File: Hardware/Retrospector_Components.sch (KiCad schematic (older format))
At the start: 148 parts, among them J1 Conn_01x08_Male, J2 Conn_01x08_Male, J3 Conn_01x08_Male, J4 Conn_01x08_Male, J5 SWD_Header, J6 USB_B_Micro, J7 Eurorack_10_pin_power, J8 I2C_TestPoint, U1 MCP6004, U10 LD1117-3.3-4Tab, U2 TL074, U3 MCP6004, U4 IS42S16800F-7TLI, U5 STM32H743ZITx, U6 TL072, U7 AS3364, U8 PCM5100APW, U9 LM2675M-5, Y1 8MHz 20pF

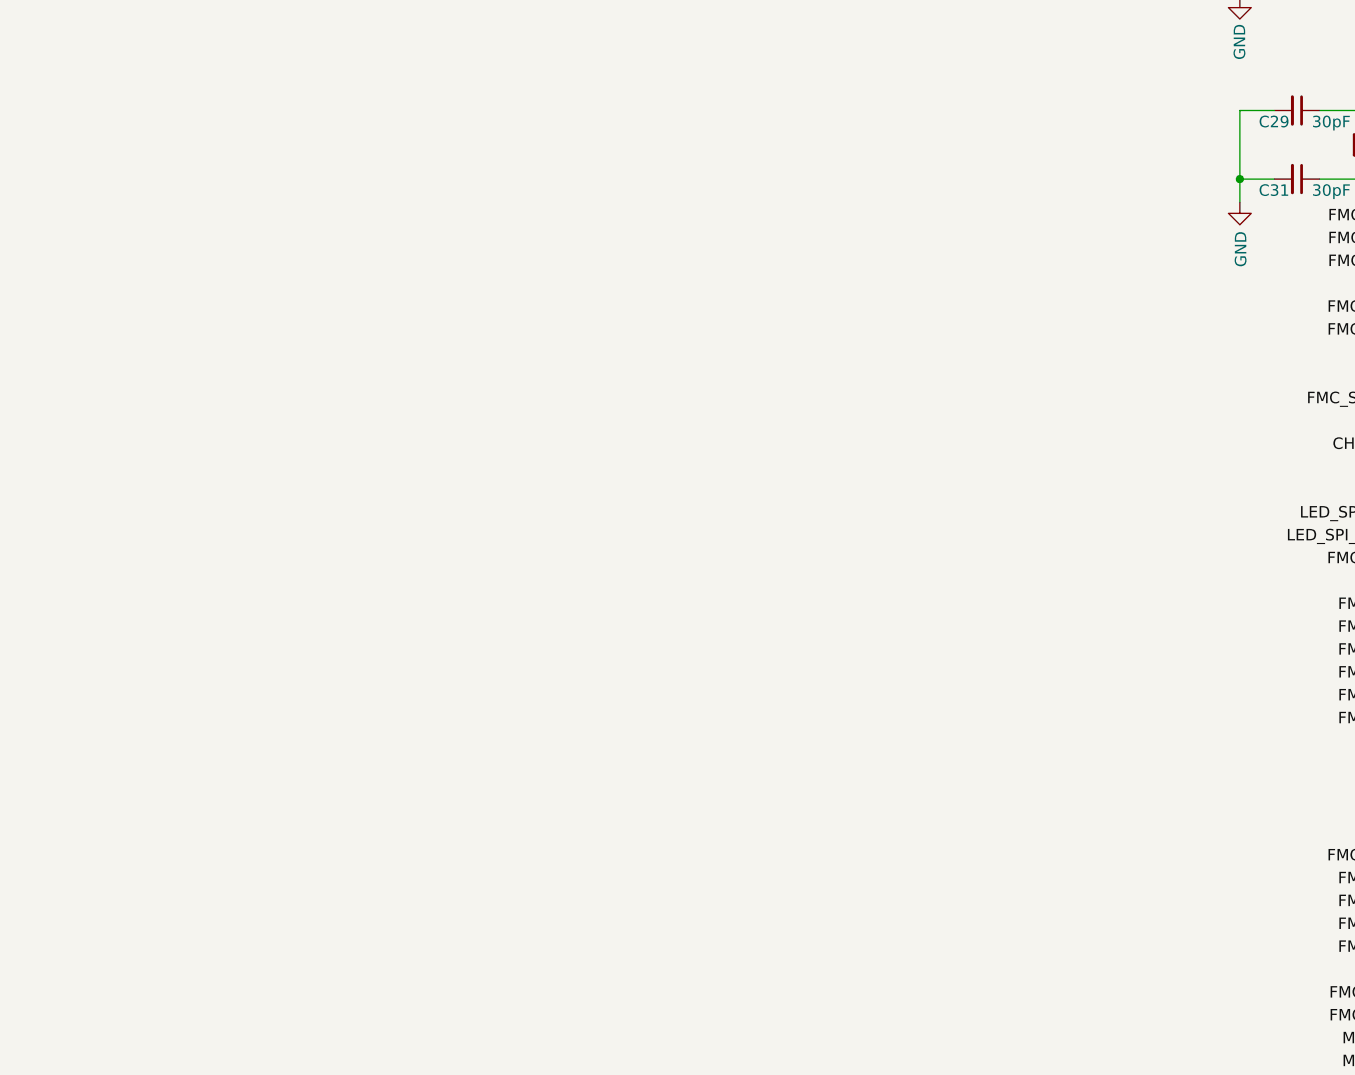
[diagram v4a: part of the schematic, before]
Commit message: Debugging ADC issues
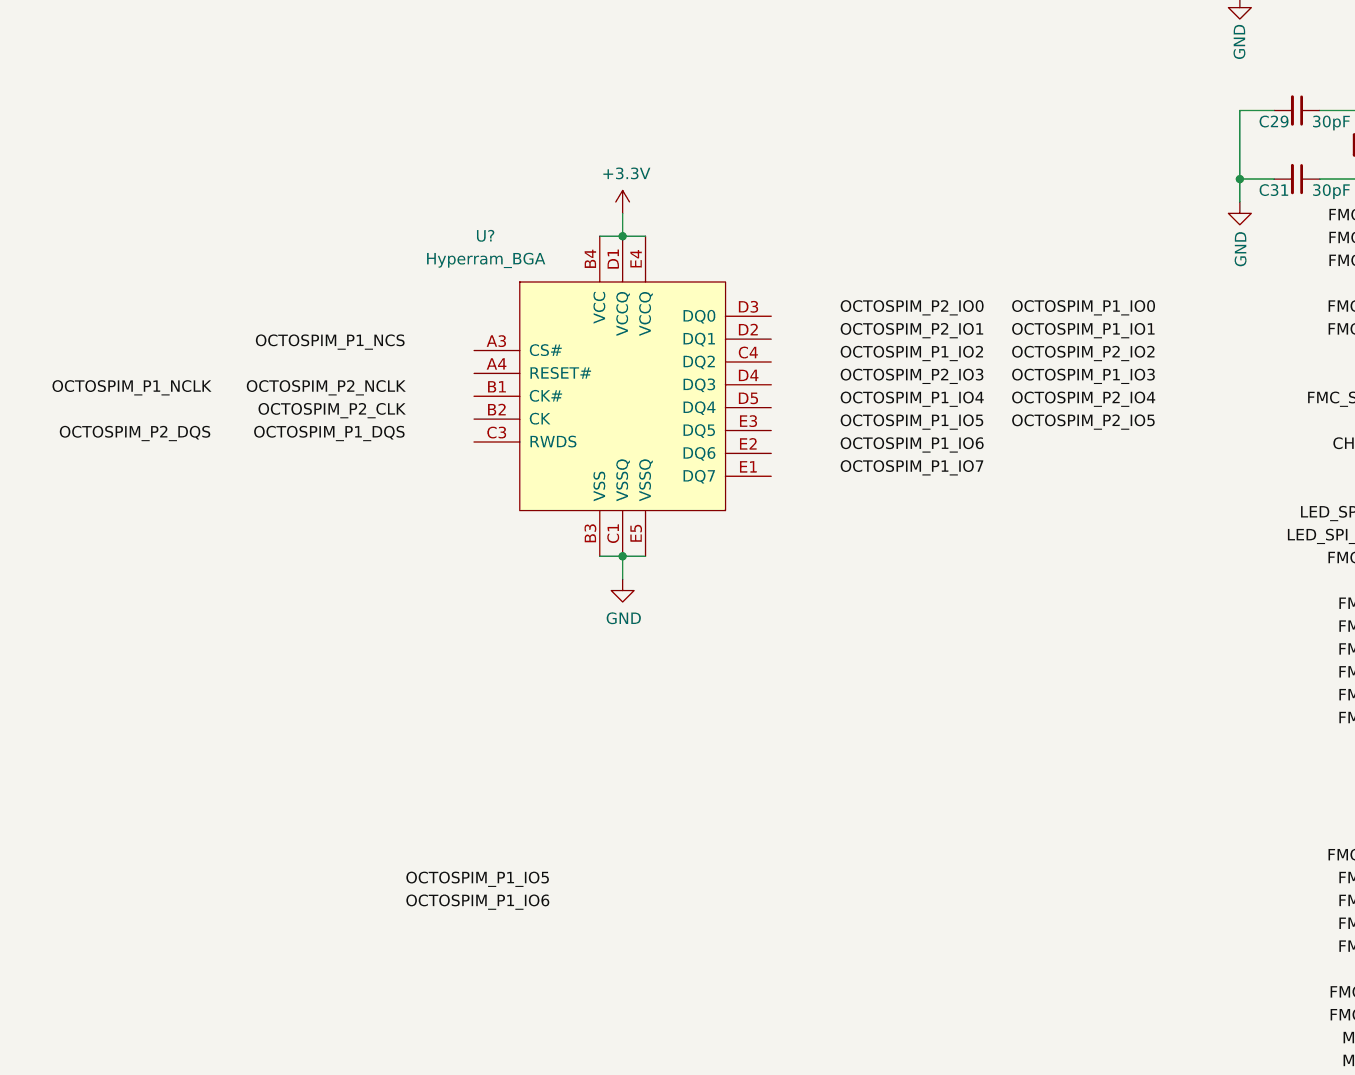
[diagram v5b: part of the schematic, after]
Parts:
- added U?: Hyperram_BGA, symbol Hyperram:Hyperram_BGA
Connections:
- net +3V3: now also U?.B4 (VCC), U?.D1 (VCCQ), U?.E4 (VCCQ)
- net GND: now also U?.B3 (VSS), U?.C1 (VSSQ), U?.E5 (VSSQ)
- new net: U?.A2 (RFU), U?.A5 (RFU), U?.B5 (RFU), U?.C2 (RFU), U?.C5 (RFU)
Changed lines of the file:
@@
 Wire Wire Line
 	1750 3850 1600 3850
+$Comp
+L Hyperram:Hyperram_BGA U?
+U 1 1 6081A4E3
+P -1800 3950
+F 0 "U?" H -2400 4200 50  0000 C CNN
+F 1 "Hyperram_BGA" H -2400 4100 50  0000 C CNN
+F 2 "" H -1950 4150 50  0001 C CNN
+F 3 "" H -1950 4150 50  0001 C CNN
+	1    -1800 3950
+	1    0    0    -1
+$EndComp
+$Comp
+L power:+3.3V #PWR?
+U 1 1 6081CB90
+P -1800 3600
+F 0 "#PWR?" H -1800 3450 50  0001 C CNN
+F 1 "+3.3V" H -1785 3773 50  0000 C CNN
+F 2 "" H -1800 3600 50  0001 C CNN
+F 3 "" H -1800 3600 50  0001 C CNN
+	1    -1800 3600
+	1    0    0    -1
+$EndComp
+Wire Wire Line
+	-1900 3700 -1800 3700
+Connection ~ -1800 3700
+Wire Wire Line
+	-1800 3700 -1700 3700
+Wire Wire Line
+	-1800 3700 -1800 3600
+$Comp
+L power:GND #PWR?
+U 1 1 6099F694
+P -1800 5200
+F 0 "#PWR?" H -1800 4950 50  0001 C CNN
+F 1 "GND" H -1795 5027 50  0000 C CNN
+F 2 "" H -1800 5200 50  0001 C CNN
+F 3 "" H -1800 5200 50  0001 C CNN
+	1    -1800 5200
+	1    0    0    -1
+$EndComp
+Wire Wire Line
+	-1900 5100 -1800 5100
+Connection ~ -1800 5100
+Wire Wire Line
+	-1800 5100 -1700 5100
+Wire Wire Line
+	-1800 5100 -1800 5200
+Text Label -850 4250 0    50   ~ 0
+OCTOSPIM_P1_IO2
+Text Label -850 4050 0    50   ~ 0
+OCTOSPIM_P2_IO0
+Text Label -850 4150 0    50   ~ 0
+OCTOSPIM_P2_IO1
+Text Label -100 4250 0    50   ~ 0
+OCTOSPIM_P2_IO2
+Text Label -850 4350 0    50   ~ 0
+OCTOSPIM_P2_IO3
+Text Label -2750 4500 2    50   ~ 0
+OCTOSPIM_P2_CLK
+Text Label -2750 4400 2    50   ~ 0
+OCTOSPIM_P2_NCLK
+Text Label -100 4350 0    50   ~ 0
+OCTOSPIM_P1_IO3
+Text Label -100 4050 0    50   ~ 0
+OCTOSPIM_P1_IO0
+Text Label -100 4150 0    50   ~ 0
+OCTOSPIM_P1_IO1
+Text Label -850 4450 0    50   ~ 0
+OCTOSPIM_P1_IO4
+Text Label -2750 6550 0    50   ~ 0
+OCTOSPIM_P1_IO5
+Text Label -2750 6650 0    50   ~ 0
+OCTOSPIM_P1_IO6
+Text Label -2750 4600 2    50   ~ 0
+OCTOSPIM_P1_DQS
+Text Label -3600 4400 2    50   ~ 0
+OCTOSPIM_P1_NCLK
+Text Label -3600 4600 2    50   ~ 0
+OCTOSPIM_P2_DQS
+Text Label -100 4450 0    50   ~ 0
+OCTOSPIM_P2_IO4
+Text Label -100 4550 0    50   ~ 0
+OCTOSPIM_P2_IO5
+Text Label -850 4550 0    50   ~ 0
+OCTOSPIM_P1_IO5
+Text Label -850 4650 0    50   ~ 0
+OCTOSPIM_P1_IO6
+Text Label -850 4750 0    50   ~ 0
+OCTOSPIM_P1_IO7
+Text Label -2750 4200 2    50   ~ 0
+OCTOSPIM_P1_NCS
 $EndSCHEMATC

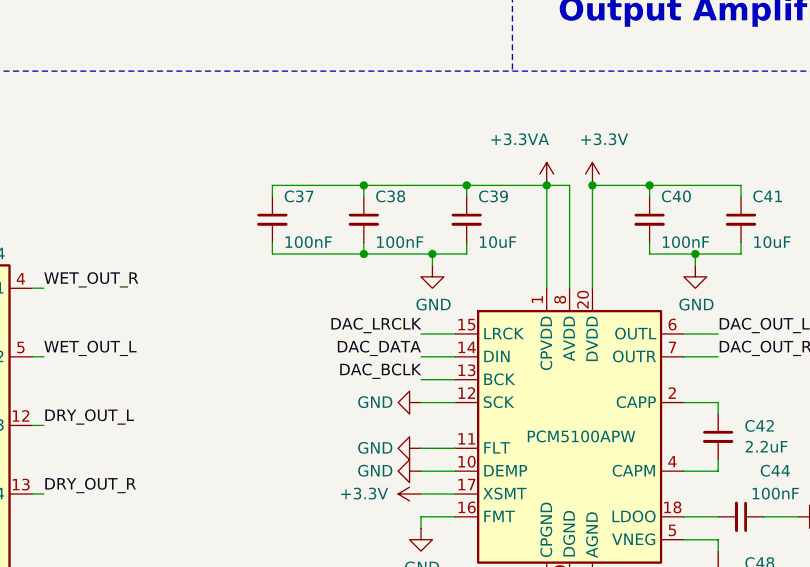
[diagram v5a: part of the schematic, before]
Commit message: Various tests for ADC accuracy
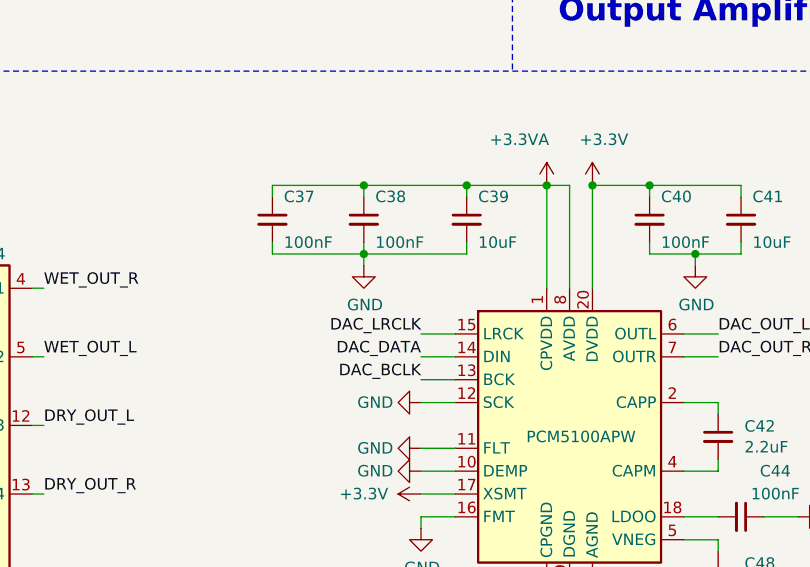
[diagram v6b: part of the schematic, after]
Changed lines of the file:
@@
 Wire Wire Line
 	13150 8600 13150 8550
-Wire Wire Line
-	13150 8850 13450 8850
 Connection ~ 13150 8850
 Wire Wire Line
@@
 L power:GND #PWR044
 U 1 1 5ED6422C
-P 13450 8900
-F 0 "#PWR044" H 13450 8650 50  0001 C CNN
-F 1 "GND" H 13455 8727 50  0000 C CNN
-F 2 "" H 13450 8900 50  0001 C CNN
-F 3 "" H 13450 8900 50  0001 C CNN
-	1    13450 8900
+P 13150 8900
+F 0 "#PWR044" H 13150 8650 50  0001 C CNN
+F 1 "GND" H 13155 8727 50  0000 C CNN
+F 2 "" H 13150 8900 50  0001 C CNN
+F 3 "" H 13150 8900 50  0001 C CNN
+	1    13150 8900
 	1    0    0    -1
 $EndComp
@@
 	1    0    0    -1
 $EndComp
-Wire Wire Line
-	13450 8900 13450 8850
-Connection ~ 13450 8850
-Wire Wire Line
-	13450 8850 13600 8850
 Wire Wire Line
 	13950 8550 13950 9000
@@
 Text Label -2750 4200 2    50   ~ 0
 OCTOSPIM_P1_NCS
+Wire Wire Line
+	13150 8850 13600 8850
+Wire Wire Line
+	13150 8850 13150 8900
 $EndSCHEMATC

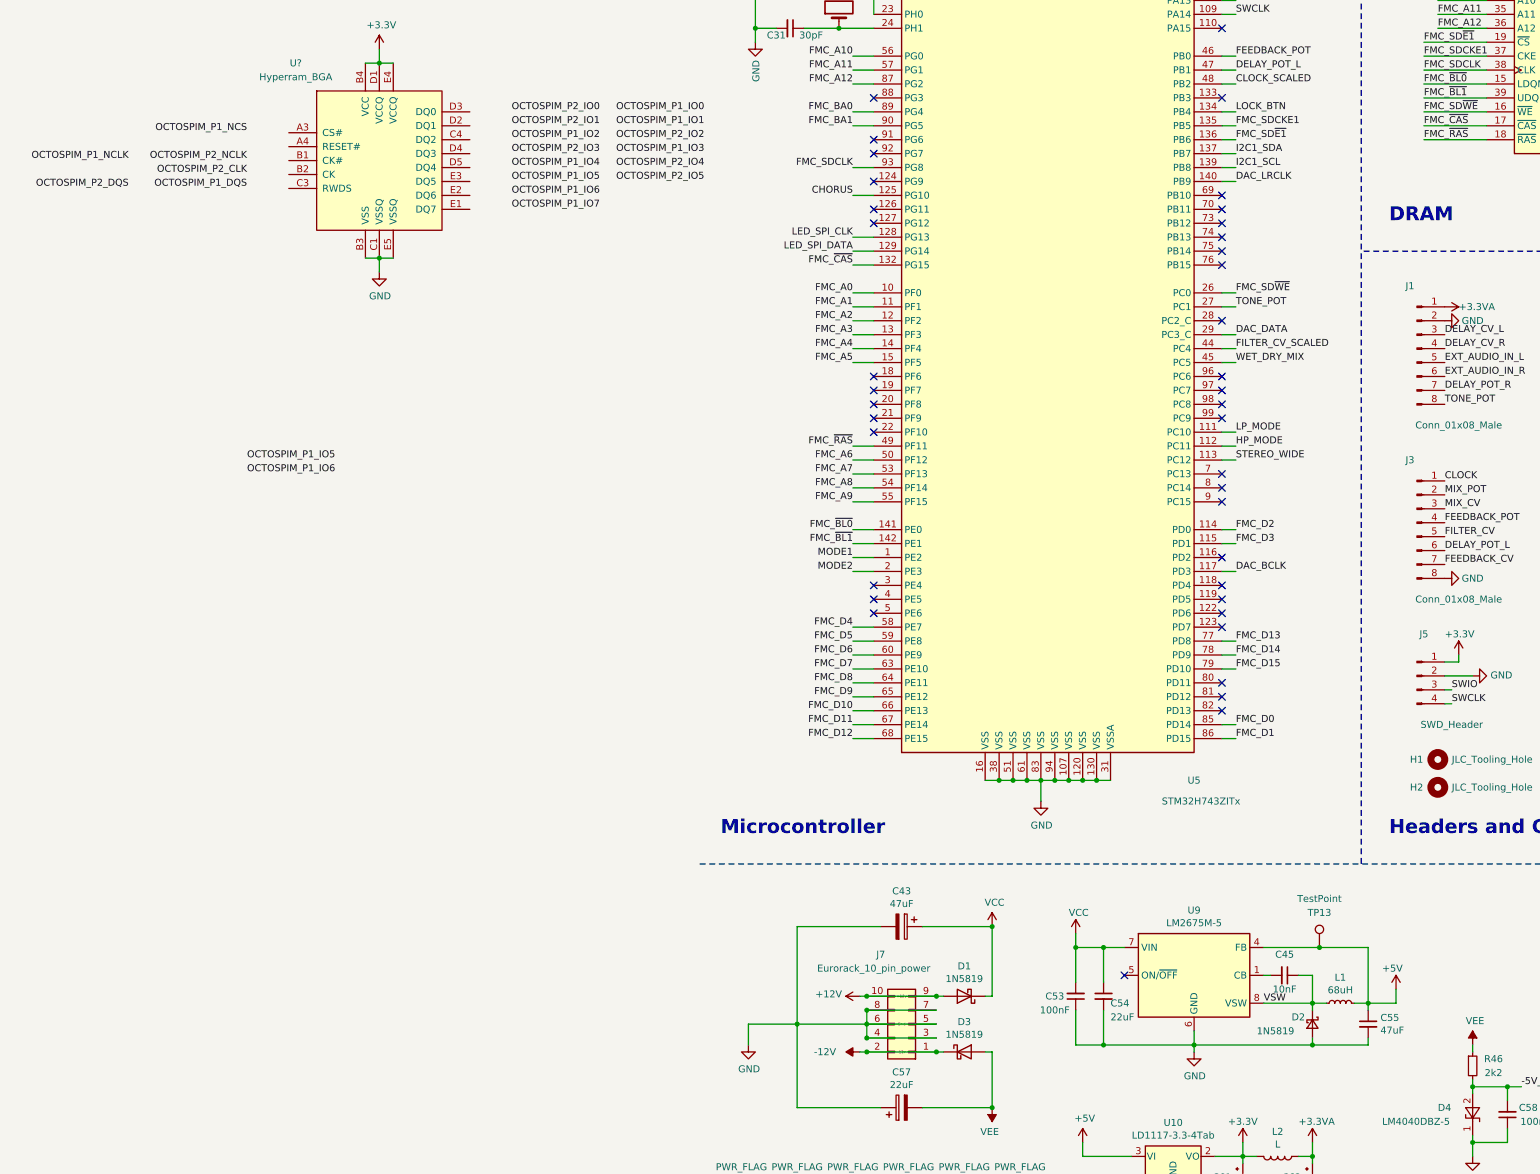
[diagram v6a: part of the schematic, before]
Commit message: Tweaks to LP filter settings; schematic
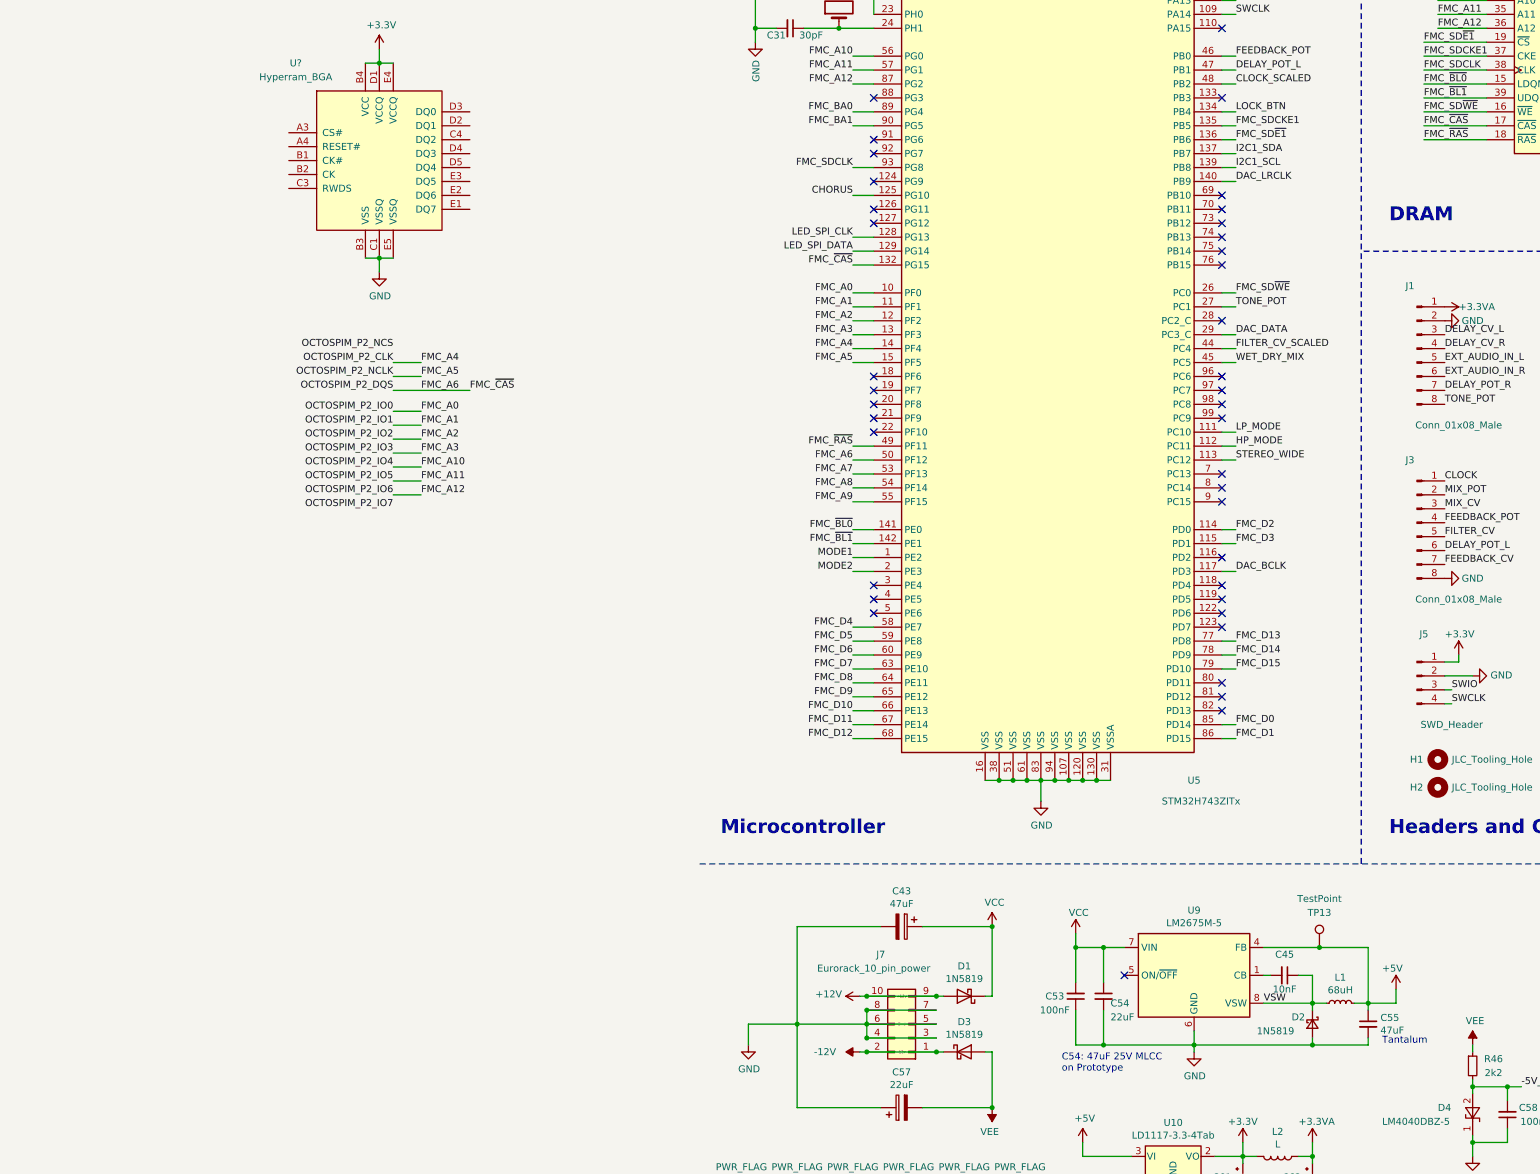
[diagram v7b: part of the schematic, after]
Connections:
- net FMC_~CAS is gone; now on net FMC_A6: U4.17 (~CAS), U5.132 (PG15)
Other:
- note added: "C54: 47uF 25V MLCC\non Prototype\n"
- note added: "Tantalum"
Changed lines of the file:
@@
 Wire Wire Line
 	-1800 5100 -1800 5200
-Text Label -850 4250 0    50   ~ 0
-OCTOSPIM_P1_IO2
-Text Label -850 4050 0    50   ~ 0
+Text Label -1700 6200 2    50   ~ 0
 OCTOSPIM_P2_IO0
-Text Label -850 4150 0    50   ~ 0
+Text Label -1700 6300 2    50   ~ 0
 OCTOSPIM_P2_IO1
-Text Label -100 4250 0    50   ~ 0
+Text Label -1700 6400 2    50   ~ 0
 OCTOSPIM_P2_IO2
-Text Label -850 4350 0    50   ~ 0
+Text Label -1700 6500 2    50   ~ 0
 OCTOSPIM_P2_IO3
-Text Label -2750 4500 2    50   ~ 0
+Text Label -1700 5850 2    50   ~ 0
 OCTOSPIM_P2_CLK
-Text Label -2750 4400 2    50   ~ 0
+Text Label -1700 5950 2    50   ~ 0
 OCTOSPIM_P2_NCLK
-Text Label -100 4350 0    50   ~ 0
-OCTOSPIM_P1_IO3
-Text Label -100 4050 0    50   ~ 0
-OCTOSPIM_P1_IO0
-Text Label -100 4150 0    50   ~ 0
-OCTOSPIM_P1_IO1
-Text Label -850 4450 0    50   ~ 0
-OCTOSPIM_P1_IO4
-Text Label -2750 6550 0    50   ~ 0
-OCTOSPIM_P1_IO5
-Text Label -2750 6650 0    50   ~ 0
-OCTOSPIM_P1_IO6
-Text Label -2750 4600 2    50   ~ 0
-OCTOSPIM_P1_DQS
-Text Label -3600 4400 2    50   ~ 0
-OCTOSPIM_P1_NCLK
-Text Label -3600 4600 2    50   ~ 0
+Text Label -1700 6050 2    50   ~ 0
 OCTOSPIM_P2_DQS
-Text Label -100 4450 0    50   ~ 0
+Text Label -1700 6600 2    50   ~ 0
 OCTOSPIM_P2_IO4
-Text Label -100 4550 0    50   ~ 0
+Text Label -1700 6700 2    50   ~ 0
 OCTOSPIM_P2_IO5
-Text Label -850 4550 0    50   ~ 0
-OCTOSPIM_P1_IO5
-Text Label -850 4650 0    50   ~ 0
-OCTOSPIM_P1_IO6
-Text Label -850 4750 0    50   ~ 0
-OCTOSPIM_P1_IO7
-Text Label -2750 4200 2    50   ~ 0
-OCTOSPIM_P1_NCS
 Wire Wire Line
 	13150 8850 13600 8850
 Wire Wire Line
 	13150 8850 13150 8900
+Text Notes 5400 10750 0    50   ~ 0
+Tantalum
+Text Notes 3100 10950 0    50   ~ 0
+C54: 47uF 25V MLCC\non Prototype\n
+Text Label -1700 6800 2    50   ~ 0
+OCTOSPIM_P2_IO6
+Text Label -1700 6900 2    50   ~ 0
+OCTOSPIM_P2_IO7
+Text Label -1700 5750 2    50   ~ 0
+OCTOSPIM_P2_NCS
+Text Label -1500 6200 0    50   ~ 0
+FMC_A0
+Text Label -1500 6300 0    50   ~ 0
+FMC_A1
+Text Label -1500 6400 0    50   ~ 0
+FMC_A2
+Text Label -1500 6500 0    50   ~ 0
+FMC_A3
+Text Label -1500 5850 0    50   ~ 0
+FMC_A4
+Text Label -1500 5950 0    50   ~ 0
+FMC_A5
+Text Label -1500 6050 0    50   ~ 0
+FMC_A6
+Text Label -1150 6050 0    50   ~ 0
+FMC_~CAS
+Text Label -1500 6600 0    50   ~ 0
+FMC_A10
+Text Label -1500 6700 0    50   ~ 0
+FMC_A11
+Text Label -1500 6800 0    50   ~ 0
+FMC_A12
+Wire Wire Line
+	-1700 5850 -1500 5850
+Wire Wire Line
+	-1700 5950 -1500 5950
+Wire Wire Line
+	-1700 6200 -1500 6200
+Wire Wire Line
+	-1700 6300 -1500 6300
+Wire Wire Line
+	-1700 6400 -1500 6400
+Wire Wire Line
+	-1700 6500 -1500 6500
+Wire Wire Line
+	-1700 6600 -1500 6600
+Wire Wire Line
+	-1700 6700 -1500 6700
+Wire Wire Line
+	-1700 6800 -1500 6800
+Wire Wire Line
+	-1700 6050 -1150 6050
 $EndSCHEMATC
